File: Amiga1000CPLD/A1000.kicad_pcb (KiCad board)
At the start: 2 copper layers, 80 x 81 mm, 13 parts, among them J1 Raspberry_Pi_2_3, J2 CSYNC IN, U1 DeniseSocket, U2 DenisePins, U3 XC9572VQ44

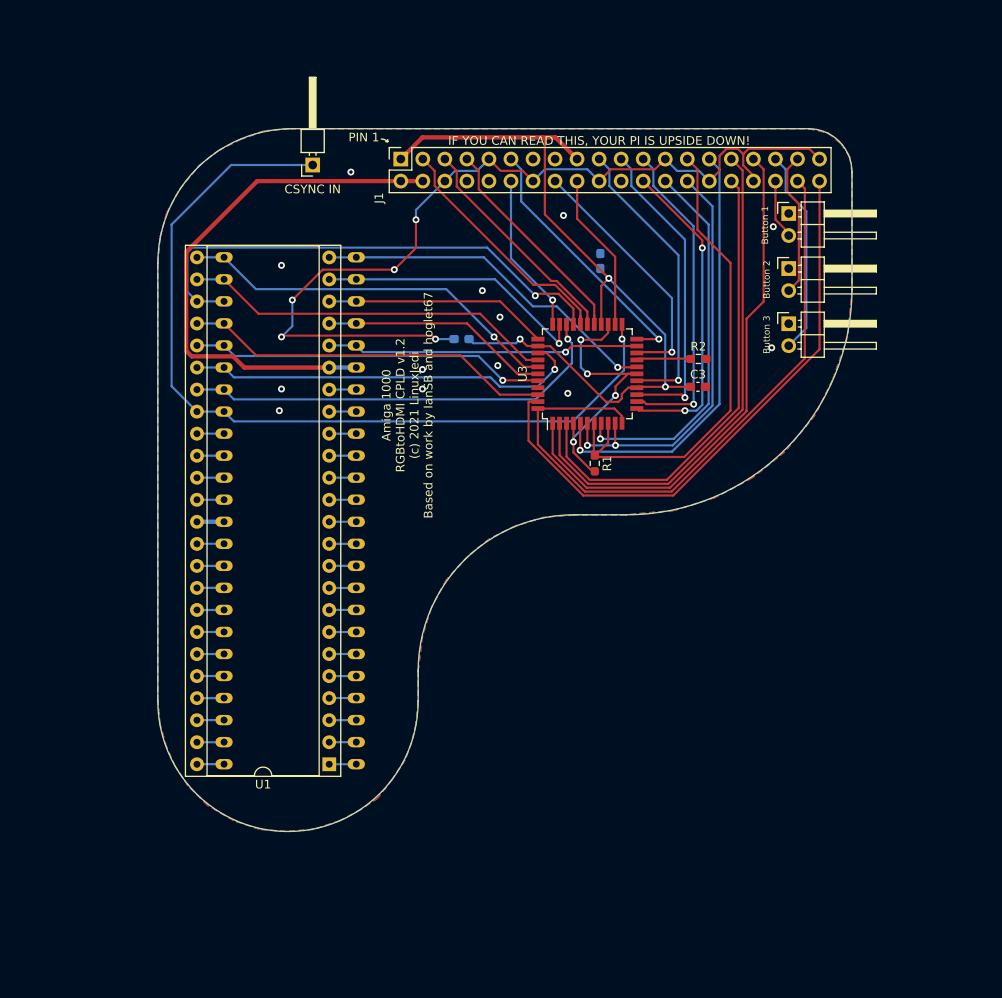
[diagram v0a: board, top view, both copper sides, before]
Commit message: Update A1000 RGBtoHDMI to rev 1.3
All SMD components are top side now. Rotated CPLD 90° for better trace
routing.
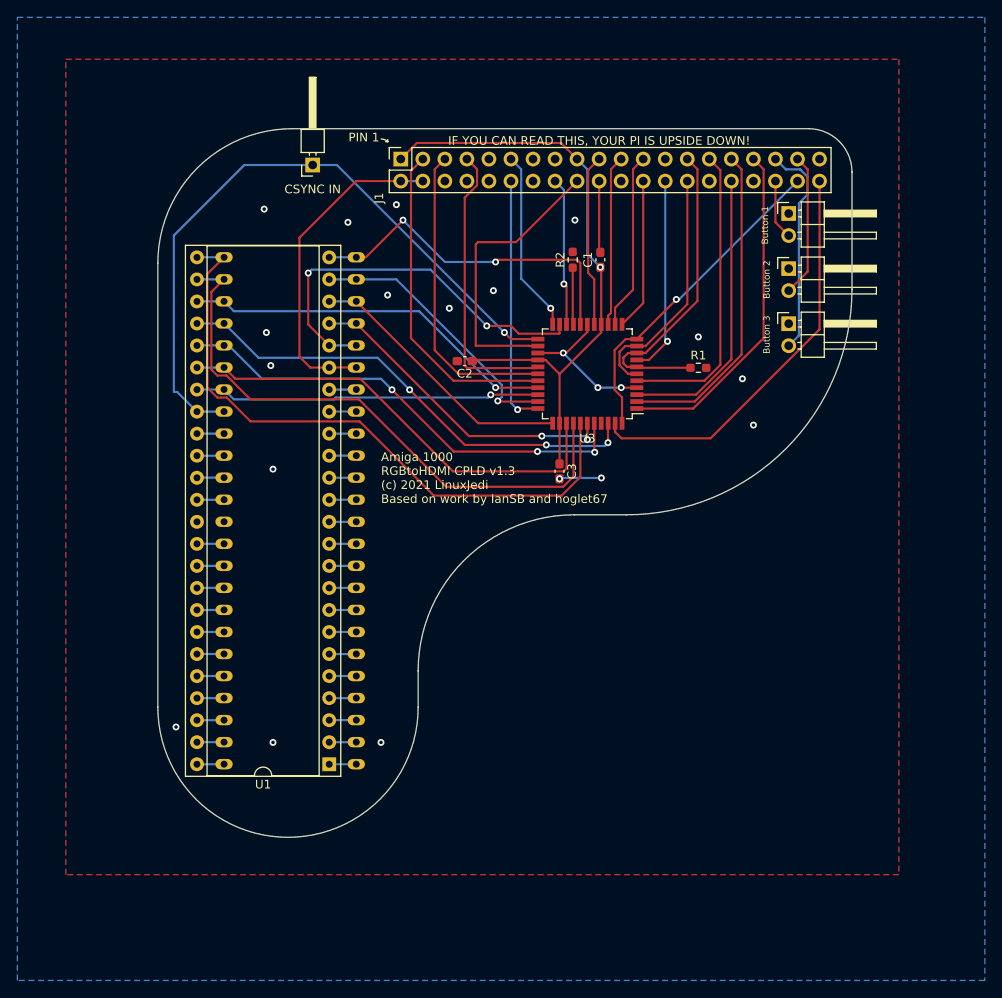
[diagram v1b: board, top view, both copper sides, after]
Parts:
- added G***: LOGO, Open68000Relocator:lxj2, F.Cu at (76.7, 62.5)
- added G***: LOGO, Open68000Relocator:lxj, F.Cu at (76.7, 62.5)
- C1, C2: moved to F.Cu
- moved C3 18.7 mm to (113.8, 94.7), turned to -90 degrees
- moved R2 18.4 mm to (115.3, 70.4), turned to 90 degrees
- moved R1 16.3 mm to (129.8, 82.8), turned to 0 degrees
- moved C2 2.57 mm to (102.9, 82.0)
- moved C1 0.14 mm to (118.5, 70.4)
- turned U3 to 180 degrees
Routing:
- net GND: track 142.0 -> 30.8 mm, vias 22 -> 21
- net /GPIO20: track 75.2 -> 37.9 mm, vias 0 -> 1
- net /B1: track 44.5 -> 74.2 mm, vias 1 -> 0
- net /B2: track 43.1 -> 68.1 mm
- net VCC: track 62.5 -> 37.7 mm
- net +3V3: track 94.2 -> 70.9 mm, vias 3 -> 1
- net /GPIO13: track 61.5 -> 39.1 mm
- net /GPIO6: track 59.1 -> 37.3 mm
- net /GPIO12: track 54.7 -> 33.1 mm
- net /HSYNC: track 99.4 -> 78.4 mm
- net /GPIO21: track 68.1 -> 47.1 mm
- net /GPIO0: track 57.5 -> 36.7 mm
- net /GPIO7: track 43.7 -> 23.0 mm
- net /CLKEN: track 48.5 -> 28.2 mm, vias 2 -> 0
- net /GPIO8: track 36.5 -> 17.5 mm, vias 2 -> 0
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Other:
- board size 80 x 81 mm -> 80 x 81.7 mm
- net class Default removed
- board text added: "Amiga 1000 RGBtoHDMI CPLD v1.3 (c) 2021 LinuxJedi Based on work by IanSB and hoglet67"
- board text removed: "Amiga 1000 RGBtoHDMI CPLD v1.2 (c) 2021 LinuxJedi Based on work by IanSB and hoglet67"

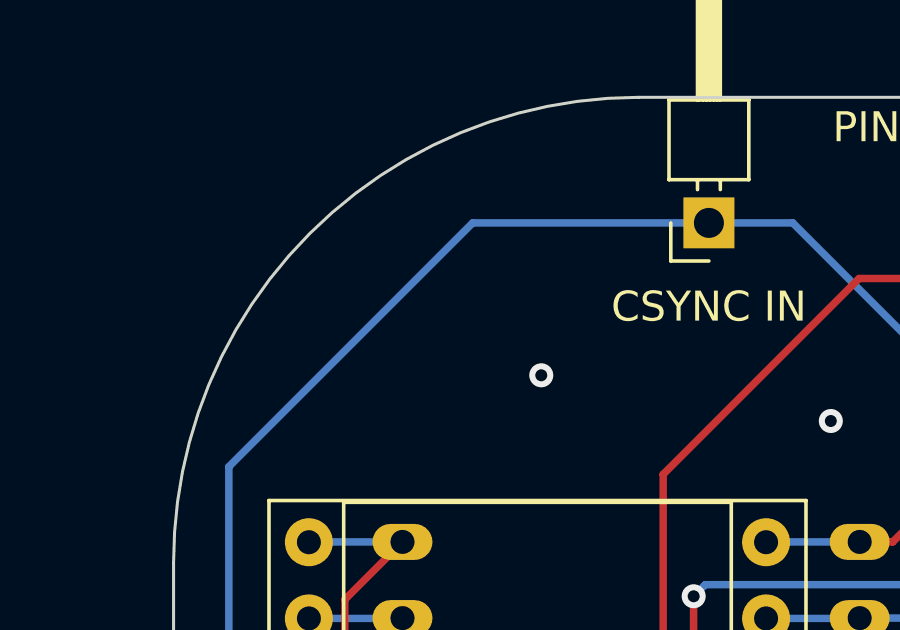
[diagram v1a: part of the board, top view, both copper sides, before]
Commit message: Add LinuxJedi logo footprints
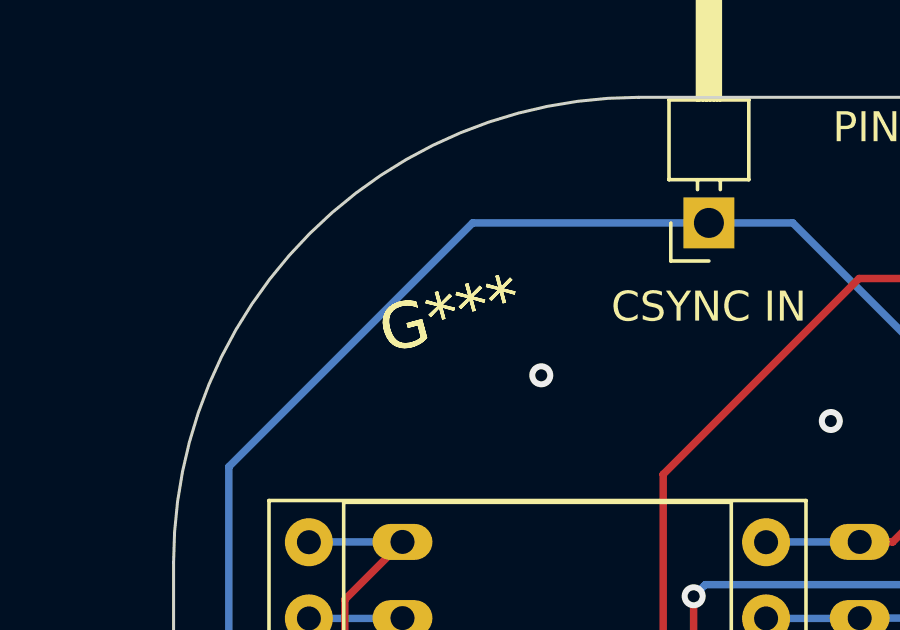
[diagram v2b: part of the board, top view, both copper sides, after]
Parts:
- G***: footprint Open68000Relocator:lxj2 -> lxj:lxj2
- G***: footprint Open68000Relocator:lxj -> lxj:lxj
